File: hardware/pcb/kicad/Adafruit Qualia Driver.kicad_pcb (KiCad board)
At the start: 2 copper layers, 45 x 85 mm, 63 parts, among them IC1 ATTINY85S, Q1 IRLR024NTRPBF, SW1 SPST_TACT-EVQQ2, SW2 SPST_TACT-EVQQ2, SW3 SPST_TACT-EVQQ2, SW4 SW_SPDT, T1 IRLML2246, T2 IRLML2246, U1 LT3754, U3 MCP16311x-xMNY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

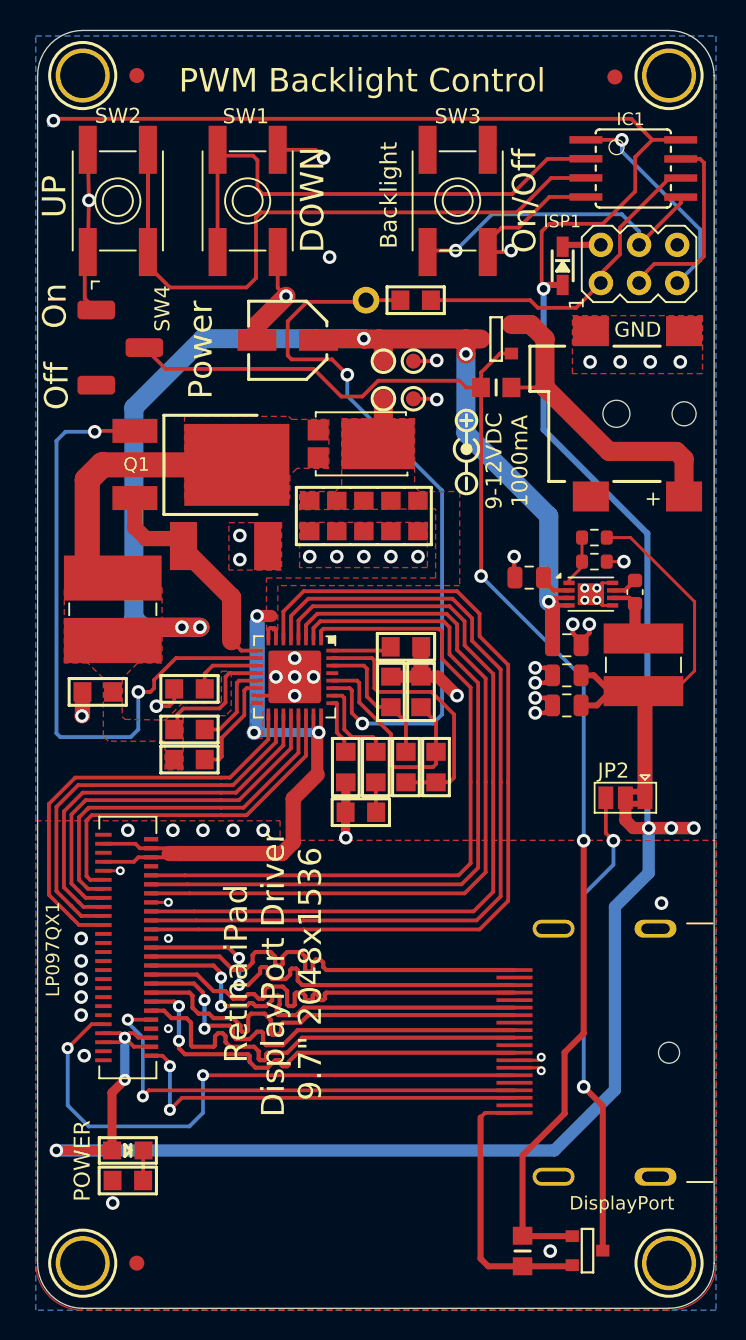
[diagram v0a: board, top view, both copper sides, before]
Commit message: update pcb silkscreen / origins
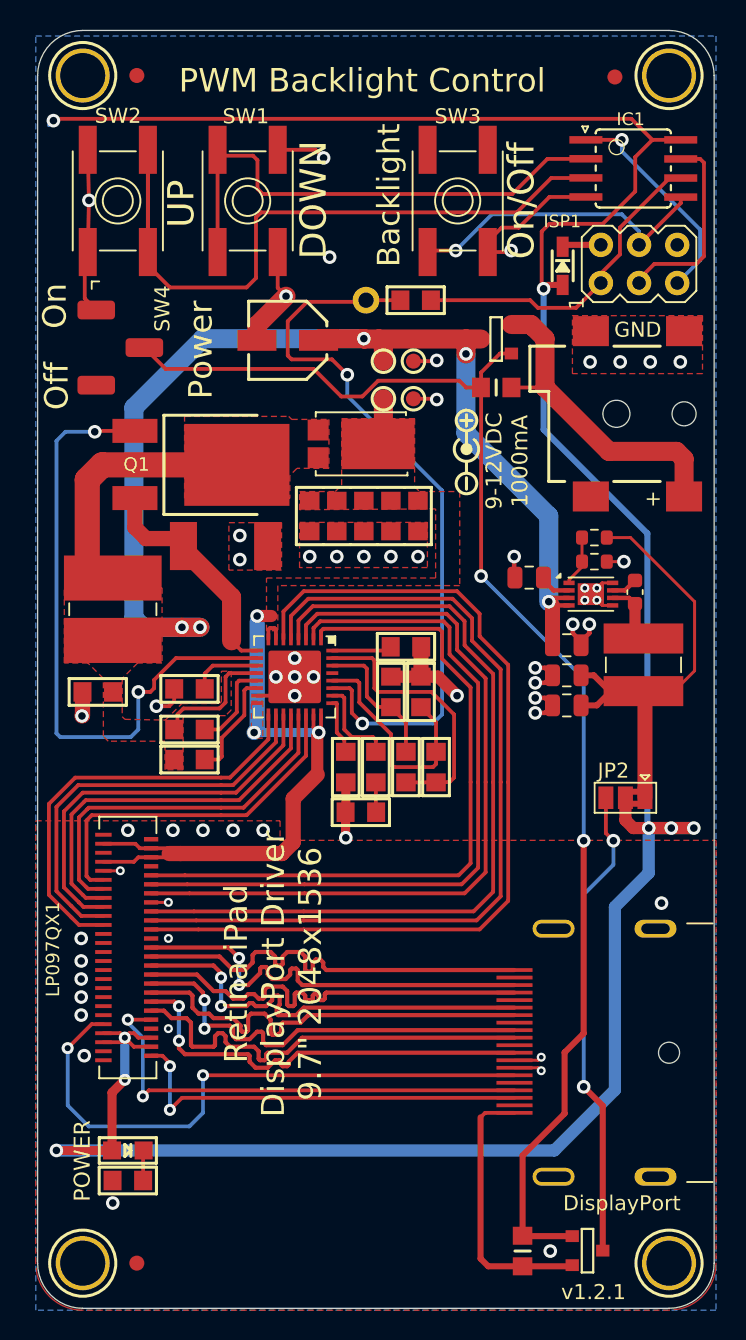
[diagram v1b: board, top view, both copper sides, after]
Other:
- board text added: "v1.2.1"
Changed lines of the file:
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@@
 		(pad_to_mask_clearance 0)
 		(allow_soldermask_bridges_in_footprints no)
+		(aux_axis_origin 125.8761 147.6286)
+		(grid_origin 125.8761 147.6286)
 		(pcbplotparams
 			(layerselection 0x00010fc_ffffffff)
 			(plot_on_all_layers_selection 0x0000000_00000000)
 			(disableapertmacros no)
-			(usegerberextensions no)
-			(usegerberattributes yes)
-			(usegerberadvancedattributes yes)
+			(usegerberextensions yes)
+			(usegerberattributes no)
+			(usegerberadvancedattributes no)
 			(creategerberjobfile yes)
 			(dashed_line_dash_ratio 12.000000)
@@
 			(drillshape 0)
 			(scaleselection 1)
-			(outputdirectory "exports/qualia_driver_pcb_v1.2.0/gerbers/")
+			(outputdirectory "exports/qualia_driver_pcb_v1.2.1/gerbers/")
 		)
 	)
@@
 		(sheetfile "Adafruit Qualia Driver.kicad_sch")
 		(fp_line
+			(start -2.8 3.4)
+			(end -2.4 3.2)
+			(stroke
+				(width 0.12)
+				(type default)
+			)
+			(layer "F.SilkS")
+		)
+		(fp_line
+			(start -2.4 3.2)
+			(end -2.8 3)
+			(stroke
+				(width 0.12)
+				(type default)
+			)
+			(layer "F.SilkS")
+		)
+		(fp_line
+			(start -2.8 3)
+			(end -2.8 3.4)
+			(stroke
+				(width 0.12)
+				(type default)
+			)
+			(layer "F.SilkS")
+		)
+		(fp_line
 			(start -2.35 2.5)
 			(end -2.34 2.5)
@@
 				(font
 					(size 1 1)
-					(thickness 0.1)
+					(thickness 0.15)
 				)
 				(justify left bottom)
@@
 	)
 	(gr_text "UP"
-		(at 128.0331 74.9866 90)
+		(at 136.5761 75.6286 90)
 		(layer "F.SilkS")
 		(effects
 			(font
-				(size 1.56464 1.56464)
-				(thickness 0.21336)
+				(size 1.75 1.75)
+				(thickness 0.25)
 			)
 			(justify left bottom)
@@
 		(effects
 			(font
-				(size 1.1176 1.1176)
-				(thickness 0.1524)
+				(size 1.5 1.5)
+				(thickness 0.2)
 			)
 		)
 	)
 	(gr_text "On/Off"
-		(at 158.3861 73.8436 90)
+		(at 158.1761 73.8286 90)
 		(layer "F.SilkS")
 		(effects
 			(font
-				(size 1.56464 1.56464)
-				(thickness 0.21336)
+				(size 1.75 1.75)
+				(thickness 0.25)
 			)
 		)
@@
 		(effects
 			(font
-				(size 0.89408 0.89408)
-				(thickness 0.12192)
+				(size 1 1)
+				(thickness 0.125)
 			)
 		)
@@
 		)
 	)
+	(gr_text "v1.2.1\n"
+		(at 162.9761 146.4286 0)
+		(layer "F.SilkS")
+		(effects
+			(font
+				(size 1 1)
+				(thickness 0.15)
+			)
+		)
+	)
 	(gr_text "Off"
 		(at 127.2711 86.1626 90)
@@
 	)
 	(gr_text "DOWN"
-		(at 145.2 77.3 90)
+		(at 145.3761 77.7286 90)
 		(layer "F.SilkS")
 		(effects
 			(font
-				(size 1.56464 1.56464)
-				(thickness 0.21336)
+				(size 1.75 1.75)
+				(thickness 0.25)
 			)
 			(justify left bottom)
